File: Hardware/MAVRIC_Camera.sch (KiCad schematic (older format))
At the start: 3 parts, among them J1 MASTER, J2 CAMERA, J3 SERVO

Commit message: Add Dynamixel servo interface
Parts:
- added C1, C2: 0.1uF, ~, symbol C
- added J4: ICSP-PIC, ~, symbol ICSP-PIC
- added J5: USB, ~, symbol USB
- added R1: 10k, ~, symbol R
- added U1: SN74HC126, symbol SN74HC126
- added U2: SN74LVC1G04, symbol SN74LVC1G04
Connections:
- net labels added: +5V, +9V, CamRx, CamTx, GND, SerDat, SerRx, SerTx, SevDr, Video
- wire segments 0 -> 36
- no-connect marks 0 -> 1
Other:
- moved on the sheet: J2

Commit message: Add servo power supply.
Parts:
- added C3: 22uF, ~, symbol CP
- added C4: 0.33uF, ~, symbol C
- added R2, R3: R, ~, symbol R
- added U3: BA00DD0W, symbol BA00DD0W
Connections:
- net labels added: +BATT, SevDat, SevEn, SevRx, SevTx
- net labels removed: SerDat, SerRx, SerTx
- wire segments 36 -> 69
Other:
- moved on the sheet: C1, C2, J3, R1

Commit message: Remove dynamixel interface, Add standard PWM
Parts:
- removed C1, C2: 0.1uF, ~, symbol C
- removed C3: 22uF, ~, symbol CP
- removed C4: 0.33uF, ~, symbol C
- removed R1: 10k, ~, symbol R
- removed R2, R3: R, ~, symbol R
- removed U1: SN74HC126, symbol SN74HC126
- removed U2: SN74LVC1G04, symbol SN74LVC1G04
- removed U3: BA00DD0W, symbol BA00DD0W
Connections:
- net labels removed: +5V, SevDat, SevDr, SevEn, SevRx, SevTx
- wire segments 69 -> 18

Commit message: Finish schematic
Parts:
- removed J5: USB, ~, symbol USB
- added C1, C15, C16, C18, C19, C2, C21, C22, C23: 22uF, ~, symbol C
- added C10, C12, C13, C14, C5, C6: 0.1uF, ~, symbol C
- added C11: 10uF, ~, symbol C
- added C17, C20, C3: C, ~, symbol C
- added C4: 10nF, ~, symbol C
- added C7: 2.2nF, ~, symbol C
- added C8, C9: 18pF, ~, symbol C
- added J5: USB_MINI, ~, symbol USB_MINI
- added L1: 33uH, ~, symbol L
- added L2, L3: 22uH, ~, symbol L
- added R1, R11, R12, R14, R15, R16, R3, R4, R9: R, ~, symbol R
- added R10, R13, R2, R5, R6, R7, R8: 10k, ~, symbol R
- added SW1: PRGM, ~, symbol SW-MOM
- added SW2: RESET, ~, symbol SW-MOM
- added U1: PIC32MX250F128D, symbol PIC32MX250F128D
- added U2: MPU9150, ~, symbol MPU9150
- added U3, U4, U5: AOZ1031, symbol AOZ1031
- added X1: 8MHz, ~, symbol CRYSTAL
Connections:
- net labels added: +3.3V, AGND, CamEn, D+, D-, OSC1, OSC2, PGC, PGD, PRGM, Pan, SCL, SDA, ServoEn, Tilt, U1Rx, U1Tx, U2Rx, U2Tx, VBus, VCap, ~MCLR
- net labels removed: +9V, CamRx, CamTx
- wire segments 18 -> 206
- no-connect marks 1 -> 7
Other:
- moved on the sheet: J1, J2, J3, J4

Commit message: Power systems layout
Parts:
- added C24, C25: 22uF, ~, symbol C
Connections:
- net labels added: CamLx, CamPwr, Lx, SevLx, SevPwr
- wire segments 206 -> 214
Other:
- moved on the sheet: C22

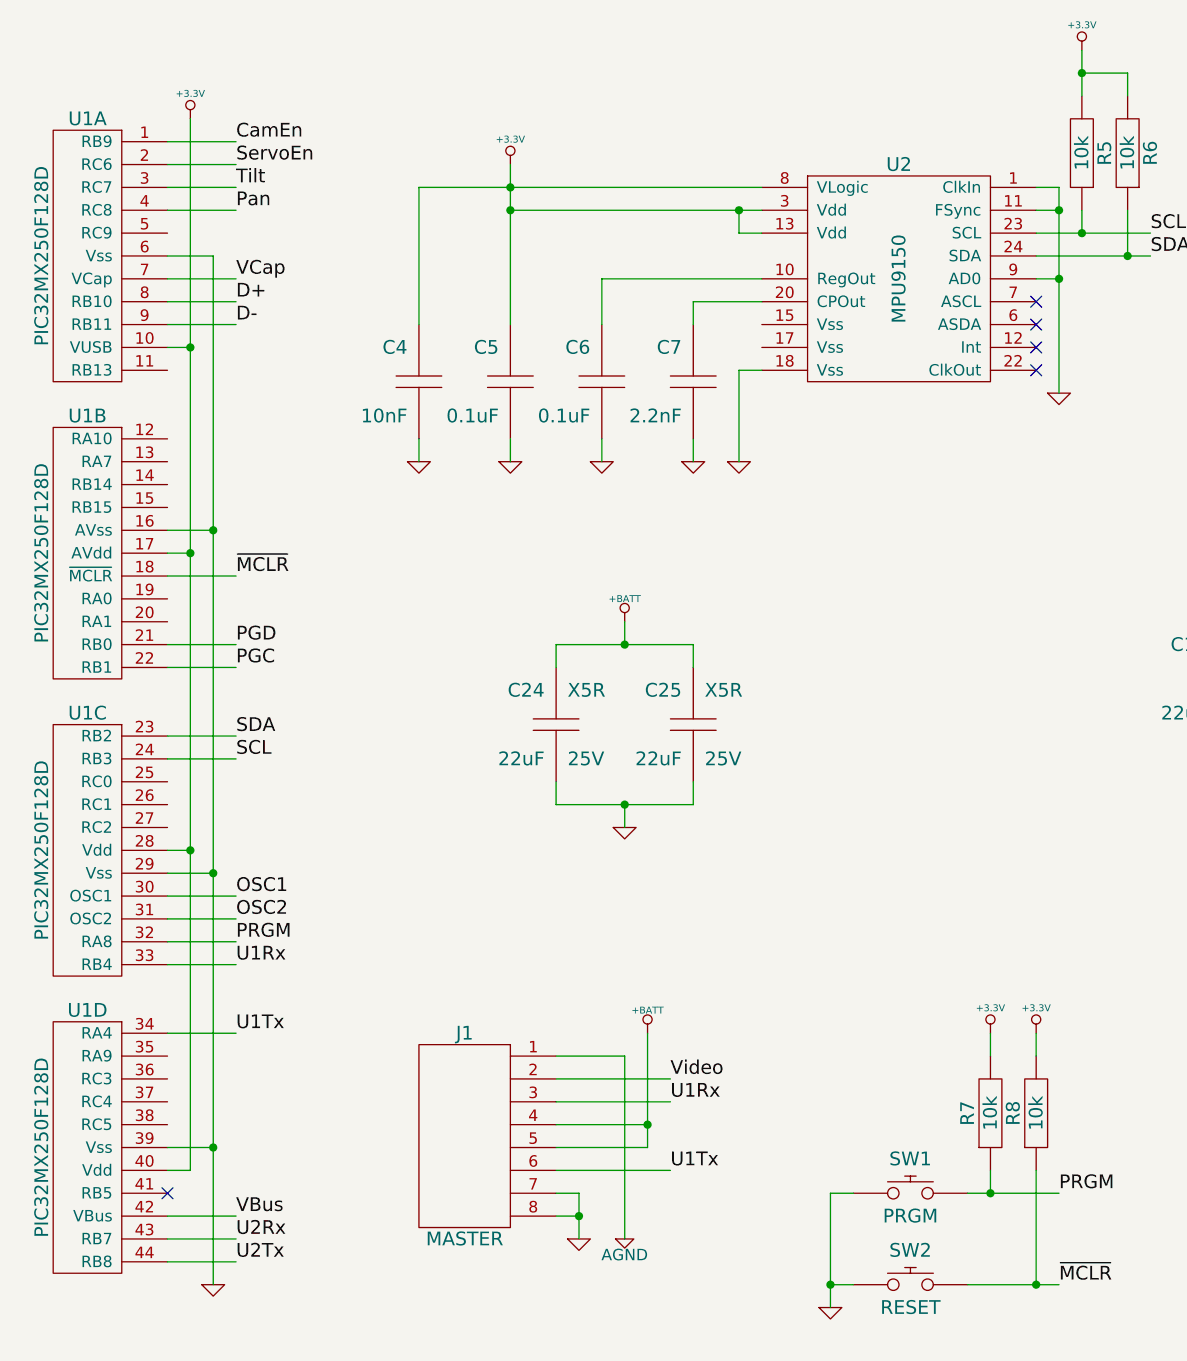
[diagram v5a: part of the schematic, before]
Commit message: New pinout. Update component layout
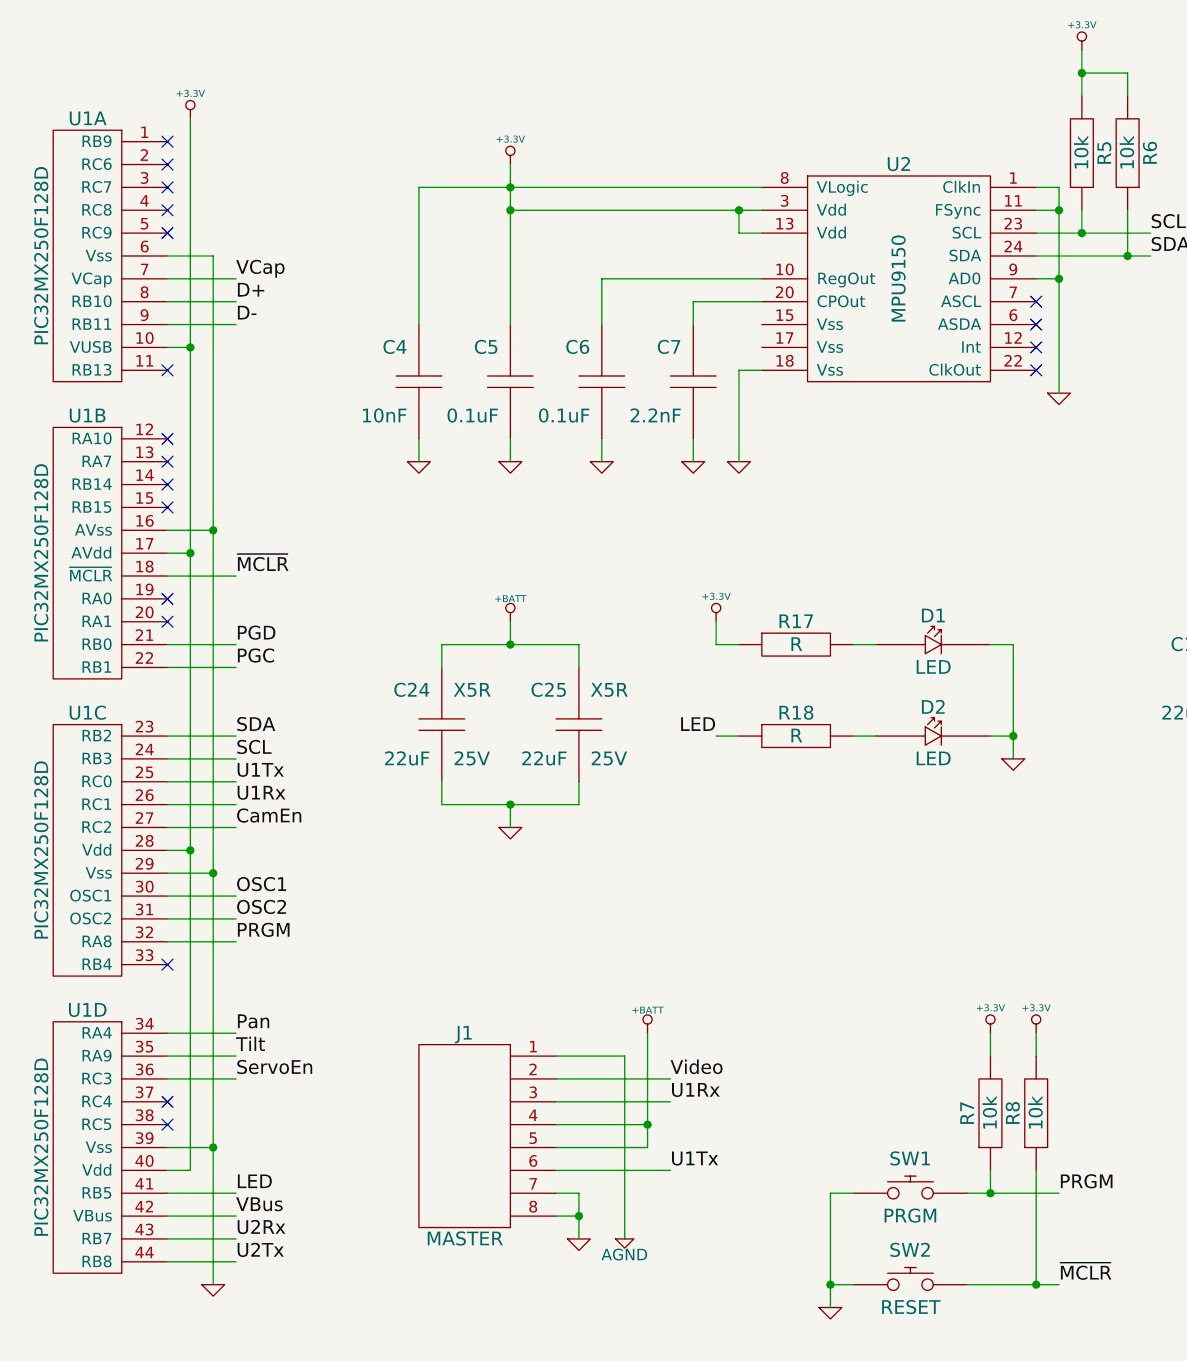
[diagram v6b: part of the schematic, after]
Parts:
- added D1, D2: LED, ~, symbol LED
- added R17, R18: R, ~, symbol R
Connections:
- net labels added: LED
- wire segments 214 -> 223
- no-connect marks 7 -> 21
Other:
- moved on the sheet: C24, C25
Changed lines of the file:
@@
 Sheet 1 1
 Title "MAVRIC Camera Controller"
-Date "9 sep 2013"
+Date "11 sep 2013"
 Rev "1"
 Comp "Iowa State University"
@@
 Text Label 1700 4600 0    60   ~ 0
 PRGM
-Text Label 1700 4700 0    60   ~ 0
+Text Label 1700 4000 0    60   ~ 0
 U1Rx
-Text Label 1700 5000 0    60   ~ 0
+Text Label 1700 3900 0    60   ~ 0
 U1Tx
 Text Label 1700 3700 0    60   ~ 0
@@
 Text Label 1700 3400 0    60   ~ 0
 PGC
-Text Label 1700 1300 0    60   ~ 0
+Text Label 1700 5100 0    60   ~ 0
 Tilt
-Text Label 1700 1400 0    60   ~ 0
+Text Label 1700 5000 0    60   ~ 0
 Pan
-Text Label 1700 1200 0    60   ~ 0
+Text Label 1700 5200 0    60   ~ 0
 ServoEn
 $Comp
@@
 	1    0    0    -1
 $EndComp
-NoConn ~ 1400 5700
 NoConn ~ 6300 7400
 Text Label 1700 1700 0    60   ~ 0
@@
 	1    0    0    -1
 $EndComp
-Text Label 1700 1100 0    60   ~ 0
+Text Label 1700 4100 0    60   ~ 0
 CamEn
 $Comp
@@
 	1700 4600 1400 4600
 Wire Wire Line
-	1700 4700 1400 4700
-Wire Wire Line
-	1400 5000 1700 5000
-Wire Wire Line
-	1700 5900 1400 5900
-Wire Wire Line
-	1700 6000 1400 6000
-Wire Wire Line
 	1400 3700 1700 3700
 Wire Wire Line
@@
 Wire Wire Line
 	7300 1000 7500 1000
-Wire Wire Line
-	1400 1100 1700 1100
-Wire Wire Line
-	1400 1200 1700 1200
-Wire Wire Line
-	1400 1300 1700 1300
-Wire Wire Line
-	1400 1400 1700 1400
 Wire Wire Line
 	1400 1800 1700 1800
@@
 L C C24
 U 1 1 522D44D8
-P 3100 3650
-F 0 "C24" H 3150 3800 60  0000 L CNN
-F 1 "22uF" H 3150 3500 60  0000 L CNN
-F 2 "~" H 3100 3650 60  0000 C CNN
-F 3 "~" H 3100 3650 60  0000 C CNN
-F 4 "25V" H 3050 3500 60  0000 R CNN "Voltage"
-F 5 "X5R" H 3050 3800 60  0000 R CNN "Dielectric"
-	1    3100 3650
+P 2600 3650
+F 0 "C24" H 2650 3800 60  0000 L CNN
+F 1 "22uF" H 2650 3500 60  0000 L CNN
+F 2 "~" H 2600 3650 60  0000 C CNN
+F 3 "~" H 2600 3650 60  0000 C CNN
+F 4 "25V" H 2550 3500 60  0000 R CNN "Voltage"
+F 5 "X5R" H 2550 3800 60  0000 R CNN "Dielectric"
+	1    2600 3650
 	-1   0    0    -1
 $EndComp
@@
 L C C25
 U 1 1 522D44E0
-P 3700 3650
-F 0 "C25" H 3750 3800 60  0000 L CNN
-F 1 "22uF" H 3750 3500 60  0000 L CNN
-F 2 "~" H 3700 3650 60  0000 C CNN
-F 3 "~" H 3700 3650 60  0000 C CNN
-F 4 "25V" H 3650 3500 60  0000 R CNN "Voltage"
-F 5 "X5R" H 3650 3800 60  0000 R CNN "Dielectric"
-	1    3700 3650
+P 3200 3650
+F 0 "C25" H 3250 3800 60  0000 L CNN
+F 1 "22uF" H 3250 3500 60  0000 L CNN
+F 2 "~" H 3200 3650 60  0000 C CNN
+F 3 "~" H 3200 3650 60  0000 C CNN
+F 4 "25V" H 3150 3500 60  0000 R CNN "Voltage"
+F 5 "X5R" H 3150 3800 60  0000 R CNN "Dielectric"
+	1    3200 3650
 	-1   0    0    -1
 $EndComp
@@
 L GND #PWR052
 U 1 1 522D44E8
-P 3400 4100
-F 0 "#PWR052" H 3400 4100 30  0001 C CNN
-F 1 "GND" H 3400 4030 30  0001 C CNN
-F 2 "" H 3400 4100 60  0000 C CNN
-F 3 "" H 3400 4100 60  0000 C CNN
-	1    3400 4100
-	1    0    0    -1
-$EndComp
-Wire Wire Line
-	3100 3900 3100 4000
-Wire Wire Line
-	3100 4000 3700 4000
-Wire Wire Line
-	3700 4000 3700 3900
-Wire Wire Line
-	3400 4100 3400 4000
-Connection ~ 3400 4000
+P 2900 4100
+F 0 "#PWR052" H 2900 4100 30  0001 C CNN
+F 1 "GND" H 2900 4030 30  0001 C CNN
+F 2 "" H 2900 4100 60  0000 C CNN
+F 3 "" H 2900 4100 60  0000 C CNN
+	1    2900 4100
+	1    0    0    -1
+$EndComp
+Wire Wire Line
+	2600 3900 2600 4000
+Wire Wire Line
+	2600 4000 3200 4000
+Wire Wire Line
+	3200 4000 3200 3900
+Wire Wire Line
+	2900 4100 2900 4000
+Connection ~ 2900 4000
 $Comp
 L +BATT #PWR053
 U 1 1 522D4713
-P 3400 3200
-F 0 "#PWR053" H 3400 3150 20  0001 C CNN
-F 1 "+BATT" H 3400 3300 30  0000 C CNN
-F 2 "" H 3400 3200 60  0000 C CNN
-F 3 "" H 3400 3200 60  0000 C CNN
-	1    3400 3200
-	1    0    0    -1
-$EndComp
-Wire Wire Line
-	3100 3400 3100 3300
-Wire Wire Line
-	3100 3300 3700 3300
-Wire Wire Line
-	3700 3300 3700 3400
-Wire Wire Line
-	3400 3200 3400 3300
-Connection ~ 3400 3300
+P 2900 3200
+F 0 "#PWR053" H 2900 3150 20  0001 C CNN
+F 1 "+BATT" H 2900 3300 30  0000 C CNN
+F 2 "" H 2900 3200 60  0000 C CNN
+F 3 "" H 2900 3200 60  0000 C CNN
+	1    2900 3200
+	1    0    0    -1
+$EndComp
+Wire Wire Line
+	2600 3400 2600 3300
+Wire Wire Line
+	2600 3300 3200 3300
+Wire Wire Line
+	3200 3300 3200 3400
+Wire Wire Line
+	2900 3200 2900 3300
+Connection ~ 2900 3300
 Text Label 8600 800  1    60   ~ 0
 Lx
+$Comp
+L LED D1
+U 1 1 522FDBA3
+P 4750 3300
+F 0 "D1" H 4750 3425 60  0000 C CNN
+F 1 "LED" H 4750 3200 60  0000 C CNN
+F 2 "~" H 4750 3300 60  0000 C CNN
+F 3 "~" H 4750 3300 60  0000 C CNN
+	1    4750 3300
+	1    0    0    -1
+$EndComp
+$Comp
+L R R17
+U 1 1 522FDBBC
+P 4150 3300
+F 0 "R17" H 4150 3400 60  0000 C CNN
+F 1 "R" H 4150 3300 60  0000 C CNN
+F 2 "~" H 4150 3300 60  0000 C CNN
+F 3 "~" H 4150 3300 60  0000 C CNN
+	1    4150 3300
+	1    0    0    -1
+$EndComp
+$Comp
+L +3.3V #PWR054
+U 1 1 522FDBCB
+P 3800 3200
+F 0 "#PWR054" H 3800 3160 30  0001 C CNN
+F 1 "+3.3V" H 3800 3310 30  0000 C CNN
+F 2 "" H 3800 3200 60  0000 C CNN
+F 3 "" H 3800 3200 60  0000 C CNN
+	1    3800 3200
+	1    0    0    -1
+$EndComp
+Wire Wire Line
+	3800 3200 3800 3300
+Wire Wire Line
+	3800 3300 3900 3300
+Wire Wire Line
+	4400 3300 4500 3300
+$Comp
+L R R18
+U 1 1 522FDDEA
+P 4150 3700
+F 0 "R18" H 4150 3800 60  0000 C CNN
+F 1 "R" H 4150 3700 60  0000 C CNN
+F 2 "~" H 4150 3700 60  0000 C CNN
+F 3 "~" H 4150 3700 60  0000 C CNN
+	1    4150 3700
+	1    0    0    -1
+$EndComp
+$Comp
+L LED D2
+U 1 1 522FDDF9
+P 4750 3700
+F 0 "D2" H 4750 3825 60  0000 C CNN
+F 1 "LED" H 4750 3600 60  0000 C CNN
+F 2 "~" H 4750 3700 60  0000 C CNN
+F 3 "~" H 4750 3700 60  0000 C CNN
+	1    4750 3700
+	1    0    0    -1
+$EndComp
+$Comp
+L GND #PWR055
+U 1 1 522FDE08
+P 5100 3800
+F 0 "#PWR055" H 5100 3800 30  0001 C CNN
+F 1 "GND" H 5100 3730 30  0001 C CNN
+F 2 "" H 5100 3800 60  0000 C CNN
+F 3 "" H 5100 3800 60  0000 C CNN
+	1    5100 3800
+	1    0    0    -1
+$EndComp
+Wire Wire Line
+	5100 3800 5100 3300
+Wire Wire Line
+	5100 3300 5000 3300
+Wire Wire Line
+	5000 3700 5100 3700
+Connection ~ 5100 3700
+Wire Wire Line
+	4400 3700 4500 3700
+Text Label 3800 3700 2    60   ~ 0
+LED
+Wire Wire Line
+	3800 3700 3900 3700
+Text Label 1700 5700 0    60   ~ 0
+LED
+Wire Wire Line
+	1700 3900 1400 3900
+Wire Wire Line
+	1700 4000 1400 4000
+Wire Wire Line
+	1700 5900 1400 5900
+Wire Wire Line
+	1700 6000 1400 6000
+Wire Wire Line
+	1400 5000 1700 5000
+Wire Wire Line
+	1400 5100 1700 5100
+Wire Wire Line
+	1700 5200 1400 5200
+Wire Wire Line
+	1700 4100 1400 4100
+Wire Wire Line
+	1400 5700 1700 5700
+NoConn ~ 1400 1100
+NoConn ~ 1400 1200
+NoConn ~ 1400 1300
+NoConn ~ 1400 1400
+NoConn ~ 1400 1500
+NoConn ~ 1400 2400
+NoConn ~ 1400 2500
+NoConn ~ 1400 2600
+NoConn ~ 1400 2700
+NoConn ~ 1400 3100
+NoConn ~ 1400 3200
+NoConn ~ 1400 4700
+NoConn ~ 1400 5300
+NoConn ~ 1400 5400
+NoConn ~ 1400 2100
 $EndSCHEMATC

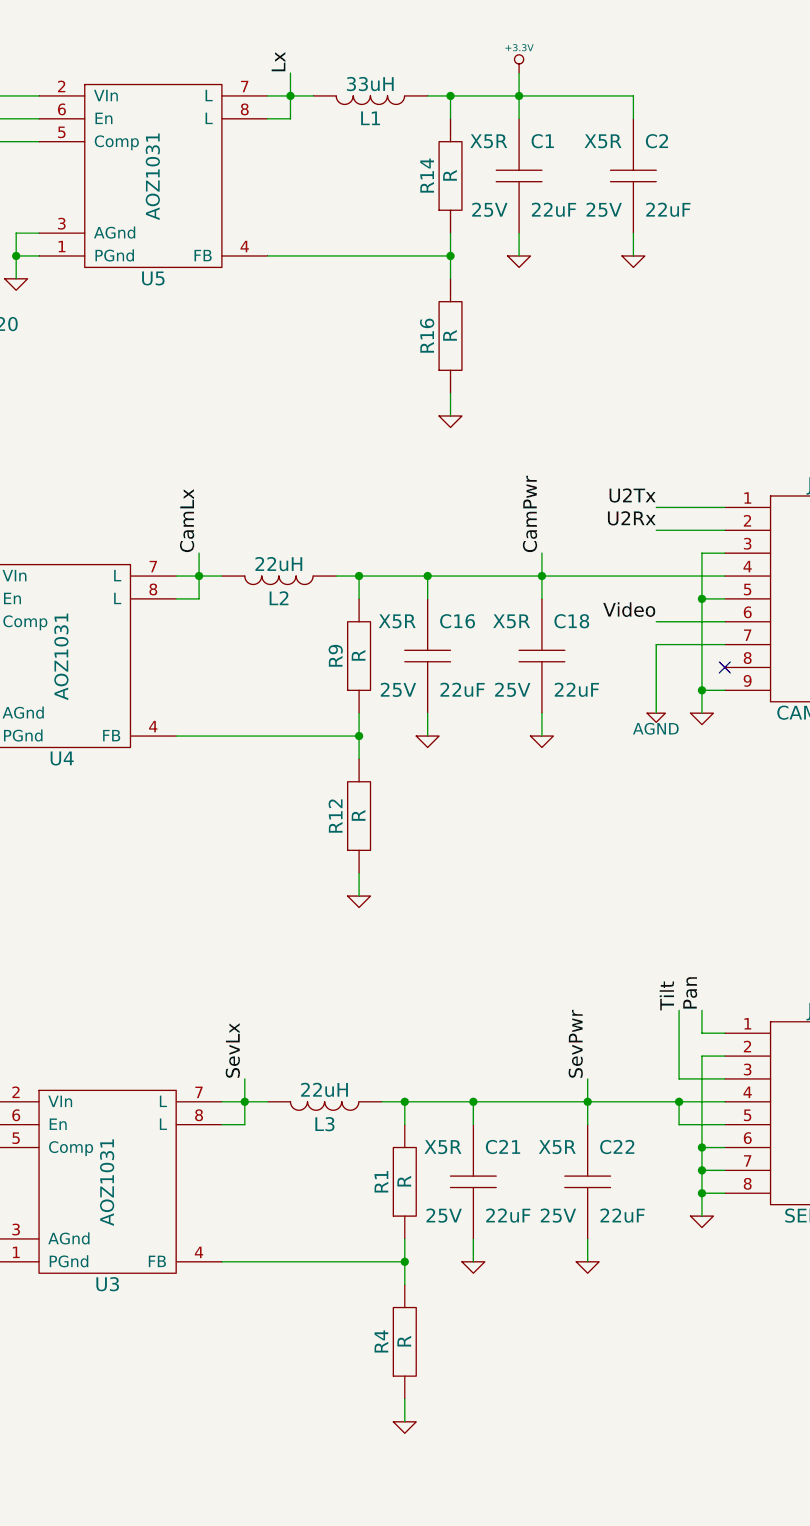
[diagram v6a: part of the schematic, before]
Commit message: Add voltage divider values
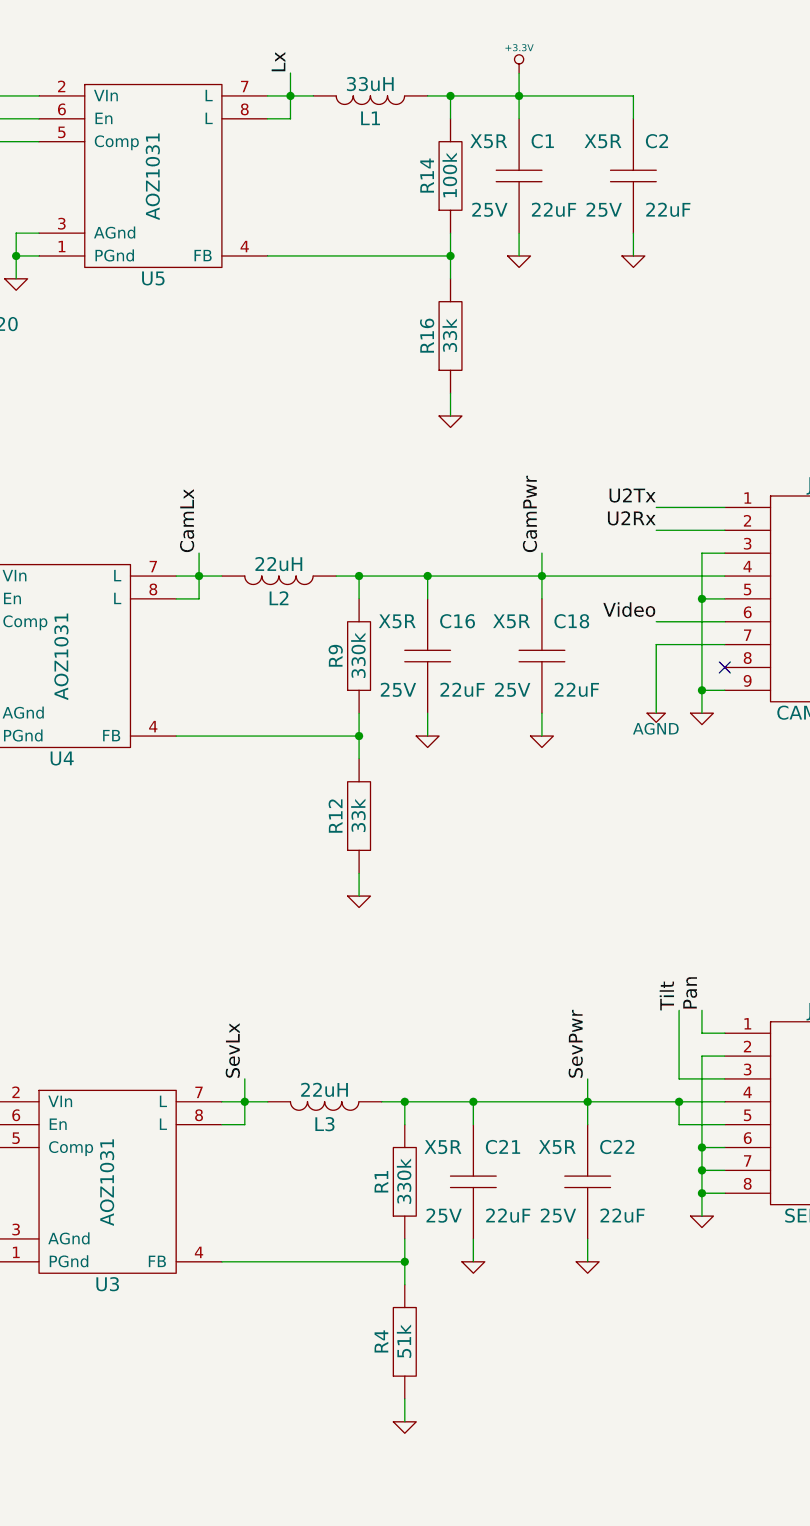
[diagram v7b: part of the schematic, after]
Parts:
- R1, R9: value R -> 330k
- R12, R16: value R -> 33k
- R14: value R -> 100k
- R4: value R -> 51k
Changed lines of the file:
@@
 Sheet 1 1
 Title "MAVRIC Camera Controller"
-Date "11 sep 2013"
+Date "28 sep 2013"
 Rev "1"
 Comp "Iowa State University"
@@
 P 9100 5650
 F 0 "R1" H 9100 5750 60  0000 C CNN
-F 1 "R" H 9100 5650 60  0000 C CNN
+F 1 "330k" H 9100 5650 60  0000 C CNN
 F 2 "~" H 9100 5650 60  0000 C CNN
 F 3 "~" H 9100 5650 60  0000 C CNN
@@
 P 9100 6350
 F 0 "R4" H 9100 6450 60  0000 C CNN
-F 1 "R" H 9100 6350 60  0000 C CNN
+F 1 "51k" H 9100 6350 60  0000 C CNN
 F 2 "~" H 9100 6350 60  0000 C CNN
 F 3 "~" H 9100 6350 60  0000 C CNN
@@
 P 8900 3350
 F 0 "R9" H 8900 3450 60  0000 C CNN
-F 1 "R" H 8900 3350 60  0000 C CNN
+F 1 "330k" H 8900 3350 60  0000 C CNN
 F 2 "~" H 8900 3350 60  0000 C CNN
 F 3 "~" H 8900 3350 60  0000 C CNN
@@
 P 8900 4050
 F 0 "R12" H 8900 4150 60  0000 C CNN
-F 1 "R" H 8900 4050 60  0000 C CNN
+F 1 "33k" H 8900 4050 60  0000 C CNN
 F 2 "~" H 8900 4050 60  0000 C CNN
 F 3 "~" H 8900 4050 60  0000 C CNN
@@
 P 9300 1250
 F 0 "R14" H 9300 1350 60  0000 C CNN
-F 1 "R" H 9300 1250 60  0000 C CNN
+F 1 "100k" H 9300 1250 60  0000 C CNN
 F 2 "~" H 9300 1250 60  0000 C CNN
 F 3 "~" H 9300 1250 60  0000 C CNN
@@
 P 9300 1950
 F 0 "R16" H 9300 2050 60  0000 C CNN
-F 1 "R" H 9300 1950 60  0000 C CNN
+F 1 "33k" H 9300 1950 60  0000 C CNN
 F 2 "~" H 9300 1950 60  0000 C CNN
 F 3 "~" H 9300 1950 60  0000 C CNN
